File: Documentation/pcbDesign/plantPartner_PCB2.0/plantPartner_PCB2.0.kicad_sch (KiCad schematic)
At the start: 67 parts, among them IC1 MPM3610, J1 Conn_01x04, J10 Screw_Terminal_01x02, J11 Conn_01x02, J12 Conn_01x03, J13 Conn_01x03, J14 Conn_01x03, J15 Conn_01x03, J16 Conn_01x01, J17 Conn_01x03, J2 Conn_01x04, J20 Conn_02x04_Top_Bottom, J21 Conn_01x04, J22 Conn_01x04, J23 Conn_01x01, J24 Conn_01x03, J26 Conn_01x01, J27 Conn_01x01, J28 Conn_01x01, J29 Conn_01x02, J3 Conn_01x04, J30 Screw_Terminal_01x02, J4 Screw_Terminal_01x04, J5 Conn_01x02, J6 Barrel_Jack, J7 Screw_Terminal_01x02, J8 Conn_02x04_Top_Bottom, J9 Screw_Terminal_01x02, Q1 AO3400A, Q2 AO3400A, Q4 AO3400A, U2 MAX485, U3 ESP32-DEVKIT-V1

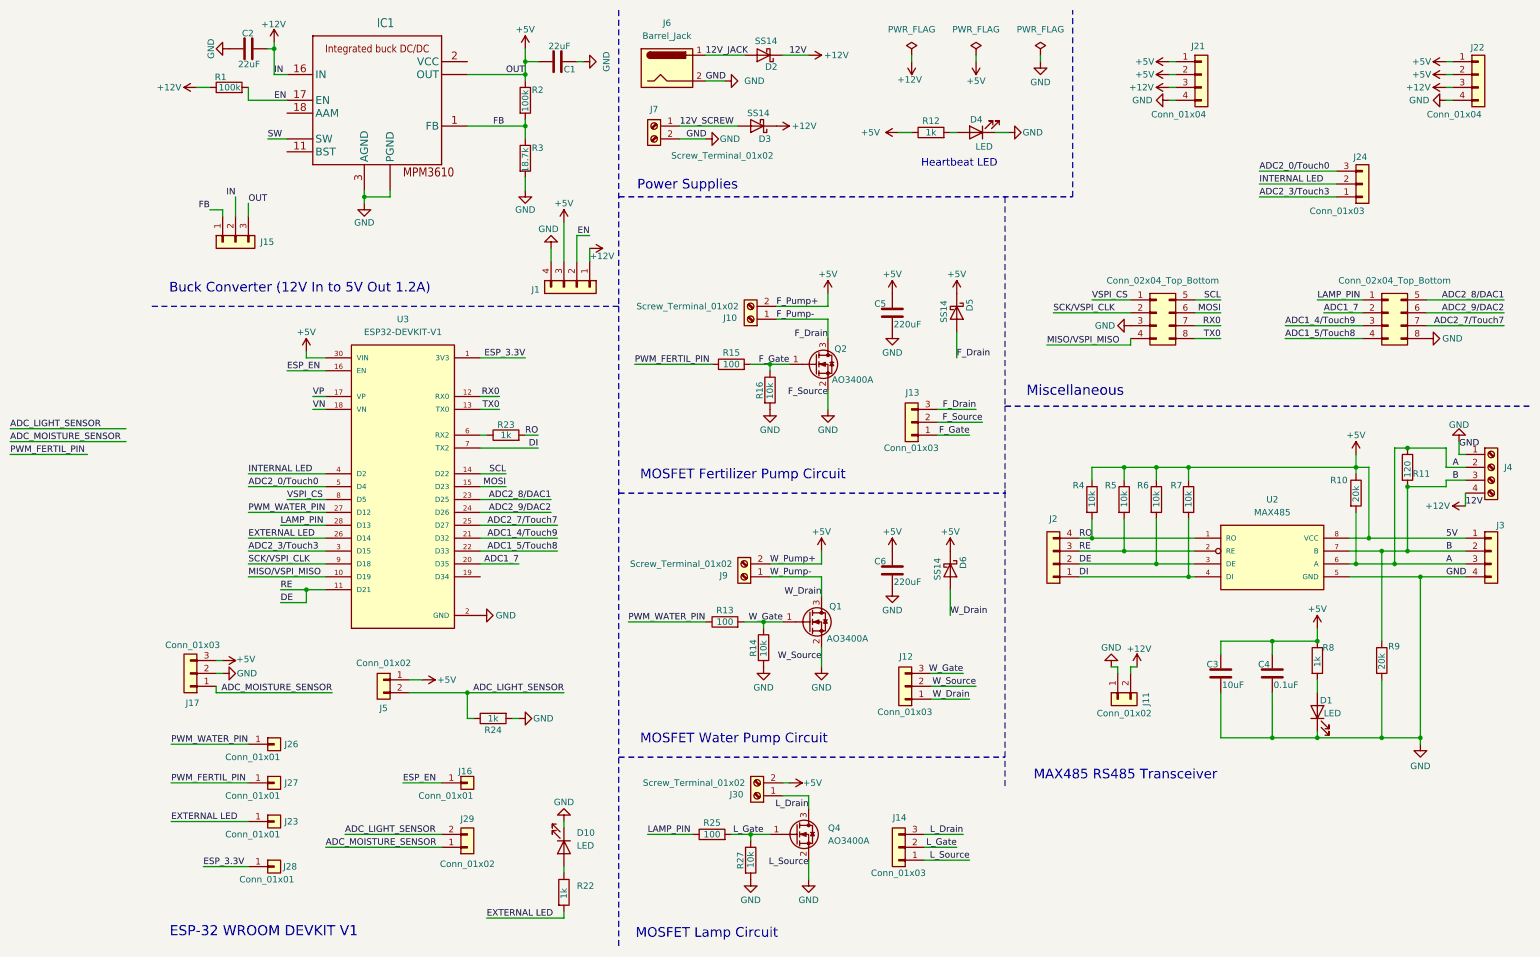
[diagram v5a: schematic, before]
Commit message: Finished routing everything. Adding silkscreens and double checking details. Next I will test in Ltspice. Hopefully, place JLC order by tonight or tomorrow
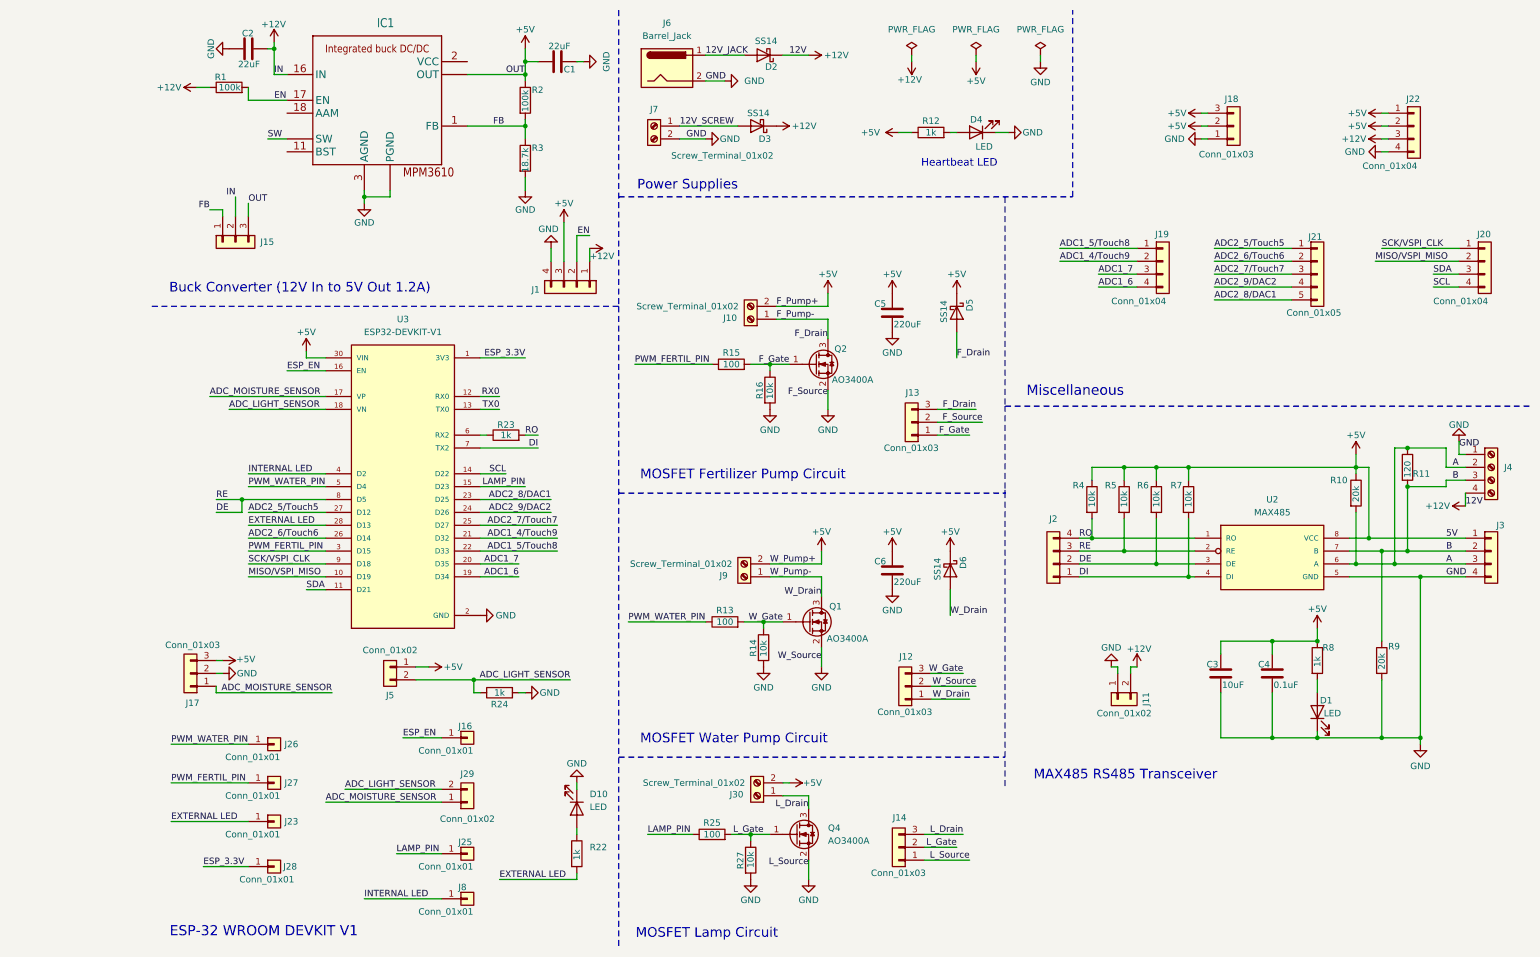
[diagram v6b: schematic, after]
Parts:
- removed J20, J8: Conn_02x04_Top_Bottom, Connector_PinHeader_2.54mm:PinHeader_2x04_P2.54mm_Vertical, symbol Connector_Generic:Conn_02x04_Top_Bottom
- removed J21: Conn_01x04, Connector_PinHeader_2.54mm:PinHeader_1x04_P2.54mm_Vertical, symbol Connector_Generic:Conn_01x04
- removed J24: Conn_01x03, Connector_PinHeader_2.54mm:PinHeader_1x03_P2.54mm_Vertical, symbol Connector_Generic:Conn_01x03
- added J18: Conn_01x03, Connector_PinHeader_2.54mm:PinHeader_1x03_P2.54mm_Vertical, symbol Connector_Generic:Conn_01x03
- added J19, J20: Conn_01x04, Connector_PinHeader_2.54mm:PinHeader_1x04_P2.54mm_Vertical, symbol Connector_Generic:Conn_01x04
- added J21: Conn_01x05, Connector_PinHeader_2.54mm:PinHeader_1x05_P2.54mm_Vertical, symbol Connector_Generic:Conn_01x05
- added J25, J8: Conn_01x01, Connector_PinHeader_2.54mm:PinHeader_1x01_P2.54mm_Vertical, symbol Connector_Generic:Conn_01x01
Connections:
- net ADC2_0/Touch0 is gone; now on net PWM_WATER_PIN: U3.5 (D4)
- net ADC2_3/Touch3 is gone; now on net PWM_FERTIL_PIN: U3.3 (D15)
- net MOSI is gone; now on net LAMP_PIN: U3.15 (D23)
- net VN is gone; now on net ADC_LIGHT_SENSOR: U3.18 (VN)
- net VP is gone; now on net ADC_MOISTURE_SENSOR: U3.17 (VP)
- net VSPI_CS is gone; now on net DE: U3.8 (D5)
- net +5V: now also J18.2 (Pin_2), J18.3 (Pin_3)
- net ADC1_4/Touch9: now also J19.2 (Pin_2)
- net ADC1_5/Touch8: now also J19.1 (Pin_1)
- net ADC1_7: now also J19.3 (Pin_3)
- net ADC2_7/Touch7: now also J21.3 (Pin_3)
- net ADC2_8/DAC1: now also J21.5 (Pin_5)
- net ADC2_9/DAC2: now also J21.4 (Pin_4)
- net DE: no longer U3.11 (D21)
- net EXTERNAL LED: now also U3.28 (D13); no longer U3.26 (D14)
- net GND: now also J18.1 (Pin_1)
- net INTERNAL LED: now also J8.1 (Pin_1)
- net LAMP_PIN: now also J25.1 (Pin_1); no longer U3.28 (D13)
- net MISO/VSPI_MISO: now also J20.2 (Pin_2)
- net PWM_WATER_PIN: no longer U3.27 (D12)
- net SCK/VSPI_CLK: now also J20.1 (Pin_1)
- net SCL: now also J20.4 (Pin_4)
- net ADC1_6: now reaches U3.19 (D34)
- net ADC1_6: now also J19.4 (Pin_4)
- new net ADC2_5/Touch5: J21.1 (Pin_1), U3.27 (D12)
- new net ADC2_6/Touch6: J21.2 (Pin_2), U3.26 (D14)
- new net SDA: J20.3 (Pin_3), U3.11 (D21)
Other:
- moved on the sheet: D10, J16, J22, J29, J5, R22, R24

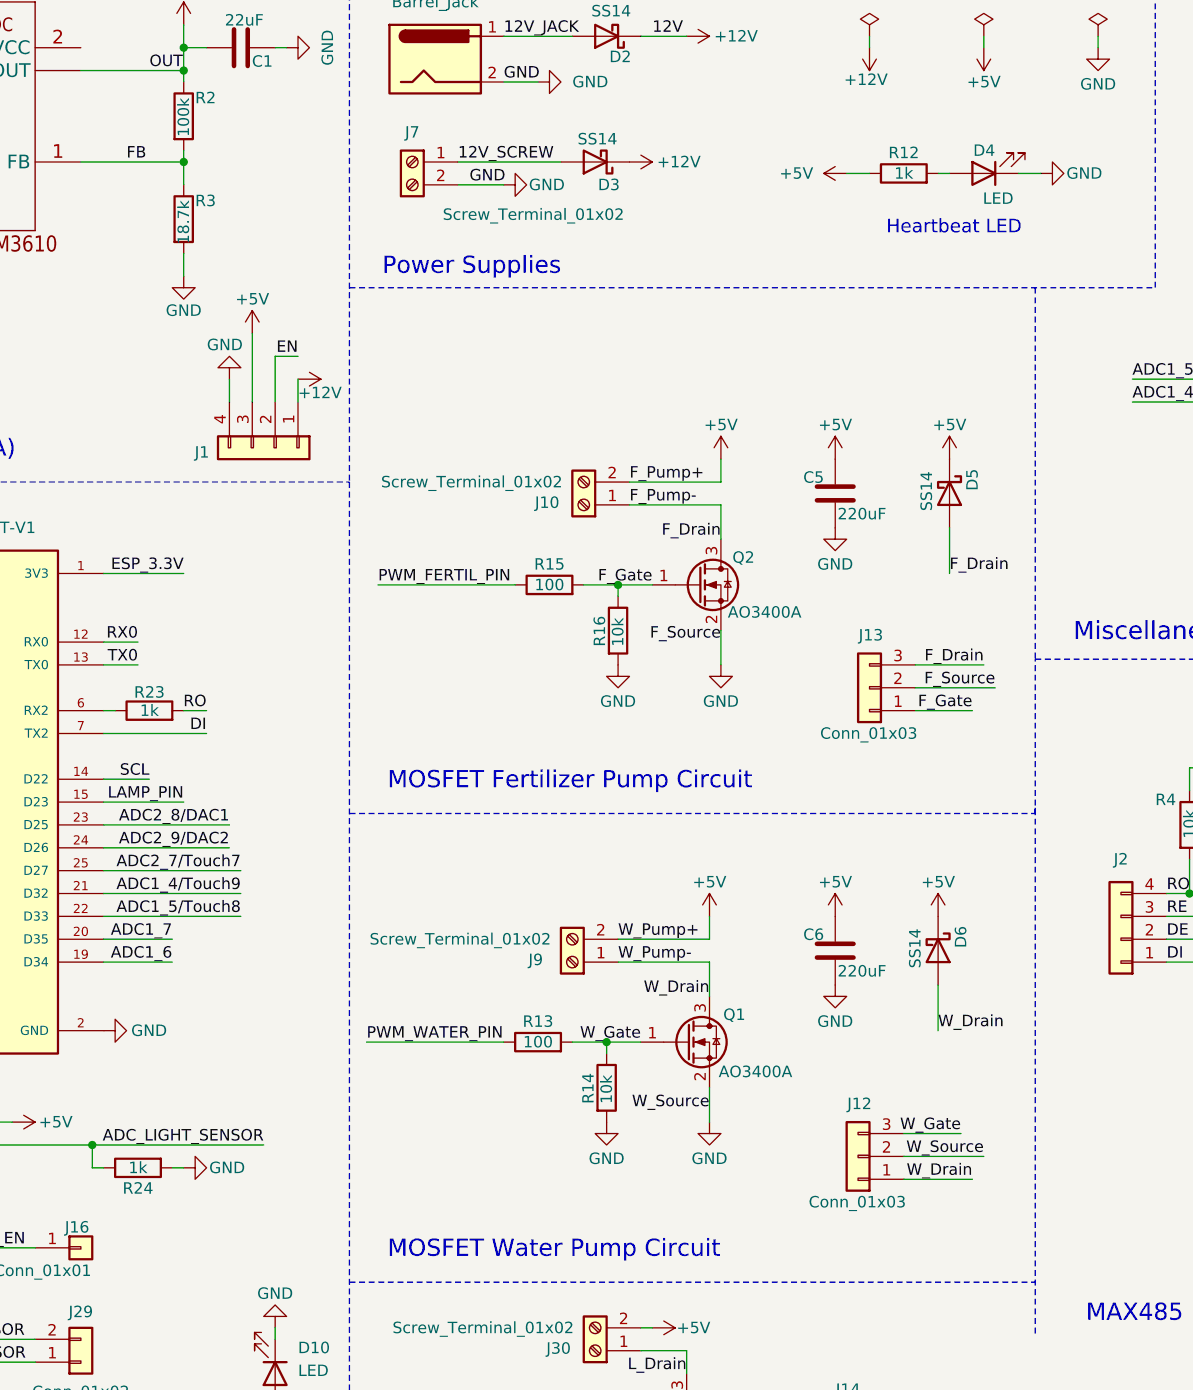
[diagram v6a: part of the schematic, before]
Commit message: Ordered PCB v2 after verifying MOSFET PWM circuits in Ltspicegit add . It was definitely cheaper but still just over 0 for all 5 to be assembled with SMT parts. Next I’ll work on “solving” the NPK so we can implement it to the entire system.
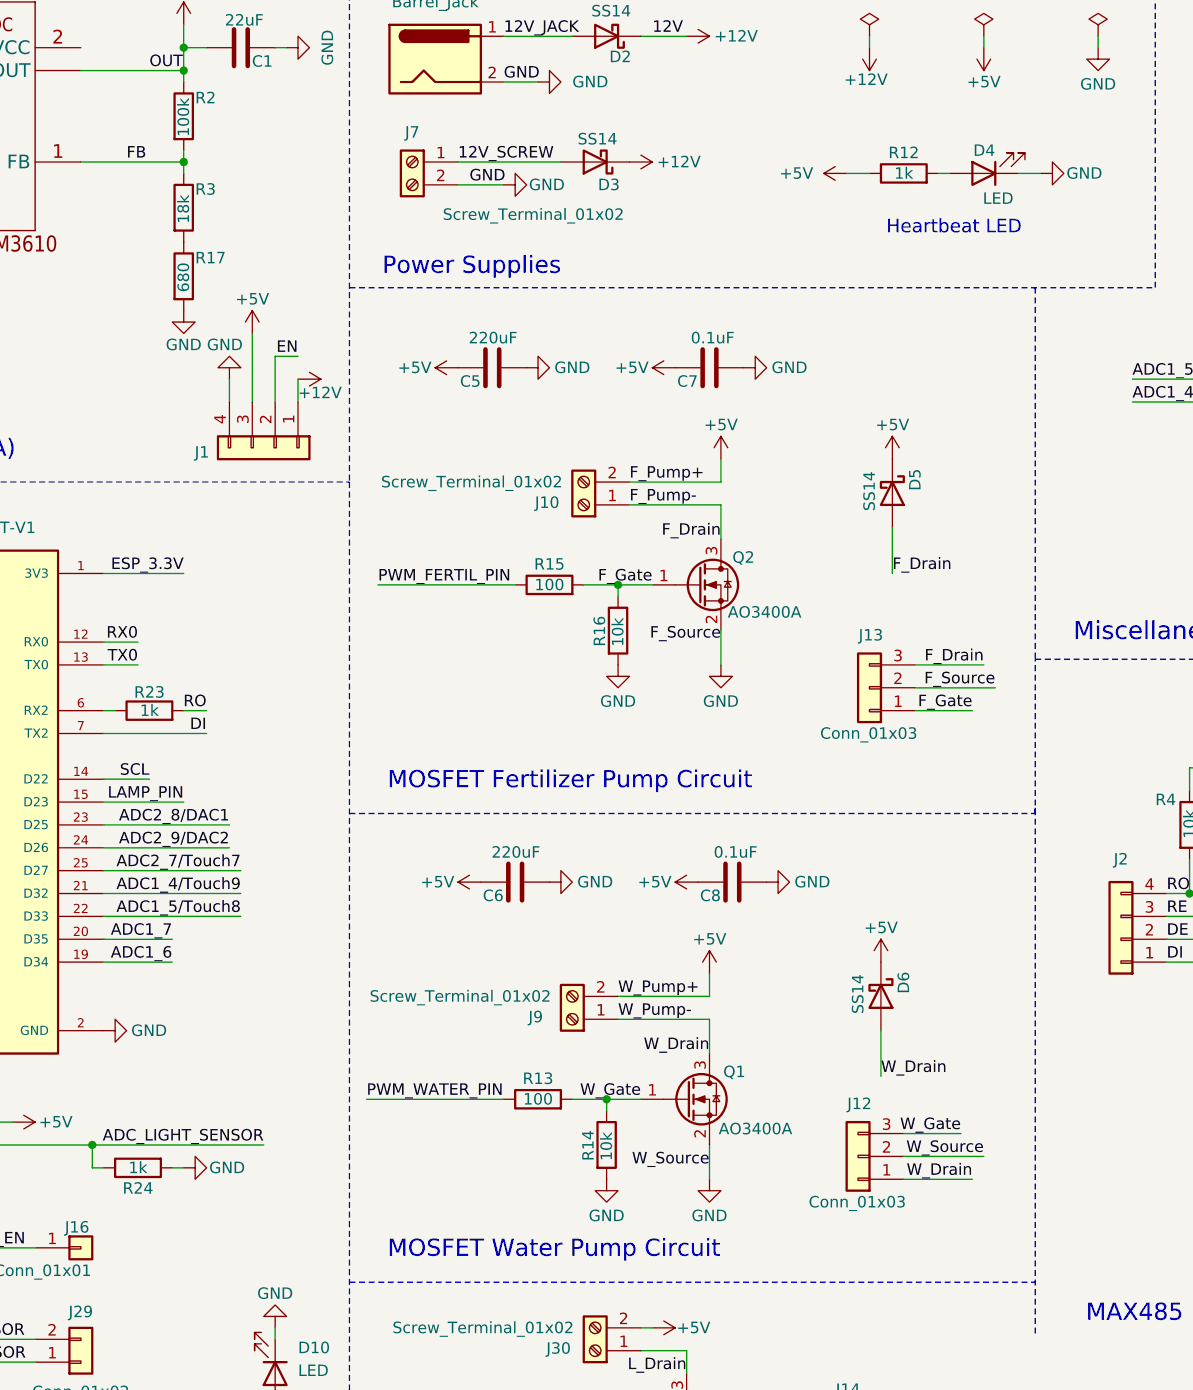
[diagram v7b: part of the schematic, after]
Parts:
- added C7, C8: 0.1uF, Capacitor_SMD:C_0603_1608Metric, symbol Device:C
- added R17: 680, Resistor_SMD:R_0603_1608Metric, symbol Device:R
- R3: value 18.7k -> 18k
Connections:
- net +5V: now also C7.1, C8.1
- net GND: now also C7.2, C8.2, R17.2; no longer R3.2
- new net: R17.1, R3.2
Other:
- moved on the sheet: C5, D5, D6, J9, Q1, R13, R14, R3

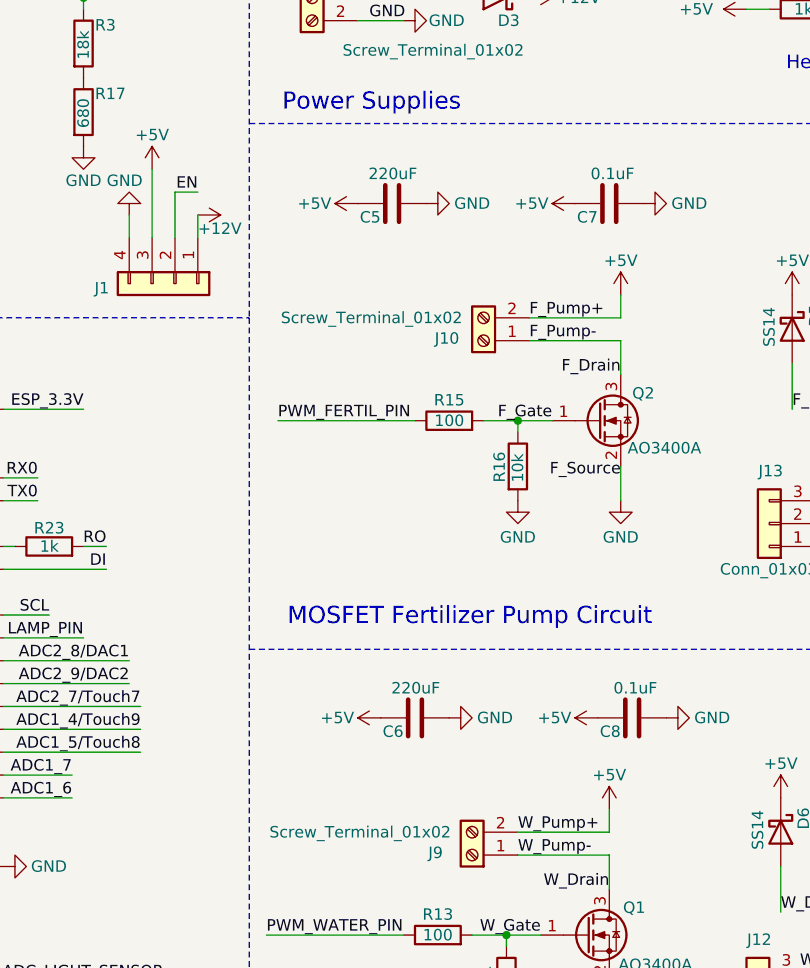
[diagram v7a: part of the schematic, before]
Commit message: I made an oopsie with PCBv2 order so I had to fix that and in the meantime I found a cheaper solution that kept the same logic of the circuits. It saved us 0 yippee
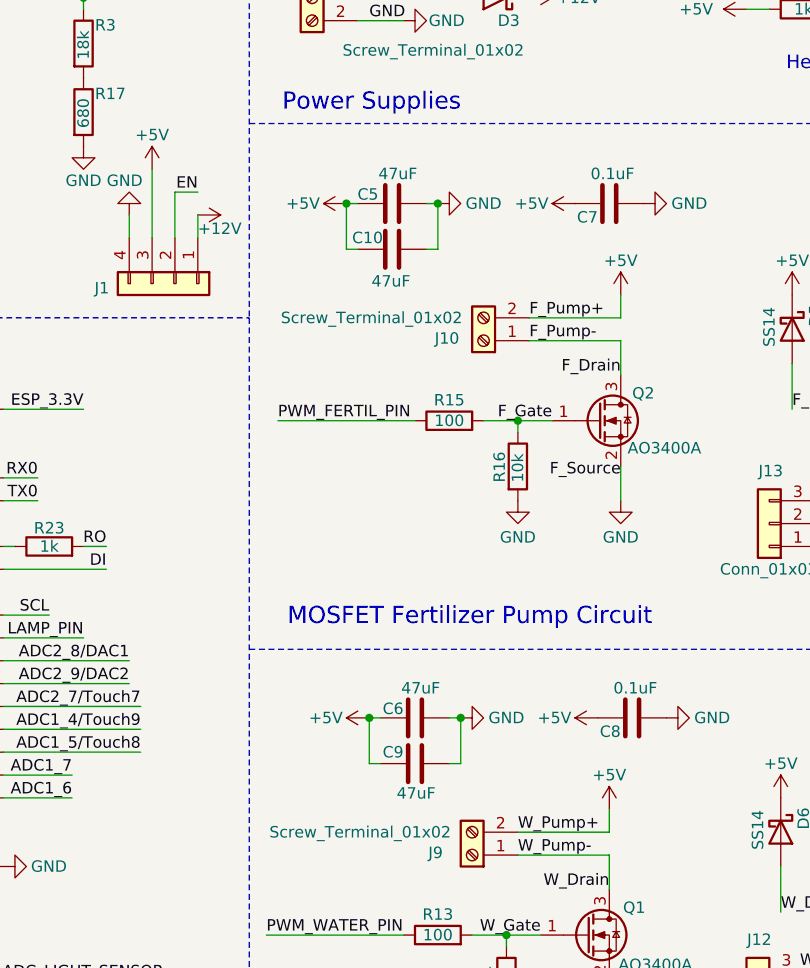
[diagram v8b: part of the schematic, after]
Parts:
- added C10, C9: 47uF, Capacitor_SMD:C_0805_2012Metric, symbol Device:C
- C5, C6: value 220uF -> 47uF; footprint Capacitor_SMD:C_0603_1608Metric -> Capacitor_SMD:C_0805_2012Metric
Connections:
- net +5V: now also C10.1, C9.1
- net GND: now also C10.2, C9.2
